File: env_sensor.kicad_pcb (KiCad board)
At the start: 2 copper layers, 43 x 63 mm, 24 parts, among them J1 E Paper, J2 ESP_Debugger, J3 Barrel_Jack, J4 LED_OUTPUT, J5 TEMP, Q1 NMOS, Q2 NMOS, Q3 NMOS, U1 MH-Z19B, U2 ESP32-DevKitC, U5 BME280

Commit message: update MOS
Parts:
- J5: value TEMP -> Conn_01x02_Pin
- Q1, Q2, Q3: footprint 2SK4017:TO230P230X650X740-3P -> env-sensor:SOT-23
- R3: value R -> 1.7k
- moved Q2 31.7 mm to (113.0, 94.7), turned to -90 degrees
- moved Q3 27.0 mm to (110.0, 98.6), turned to -90 degrees
- moved Q1 22.5 mm to (116.6, 98.3), turned to -90 degrees
- moved J4 16.0 mm to (117.6, 102.4), turned to -90 degrees
- moved C5 1.60 mm to (112.1, 72.4), turned to -90 degrees
- moved J3 1.27 mm to (124.6, 89.5)
- moved C1 0.87 mm to (111.3, 79.8)
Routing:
- net LED_C2: track 10.9 -> 31.0 mm, vias 0 -> 2
- net LED_C3: track 10.2 -> 28.1 mm, vias 0 -> 2
- net LED_V2: track 24.7 -> 6.95 mm
- net LED_C1: track 9.08 -> 25.3 mm, vias 0 -> 2
- net LED_V3: track 13.1 -> 2.80 mm
- net v12: track 24.6 -> 14.9 mm
- net LED_V1: track 10.7 -> 3.51 mm
- net GND: vias 17 -> 21

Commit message: add drv8847 (Working)
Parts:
- added R4: 330m, Resistor_SMD:R_0603_1608Metric, F.Cu at (97.5, 70.6)
- added R5: 330m, Resistor_SMD:R_0603_1608Metric, F.Cu at (97.5, 73.1)
- added U3: DRV8847SPWR, Package_SO:TSSOP-16_4.4x5mm_P0.65mm, F.Cu at (100.3, 66.1)

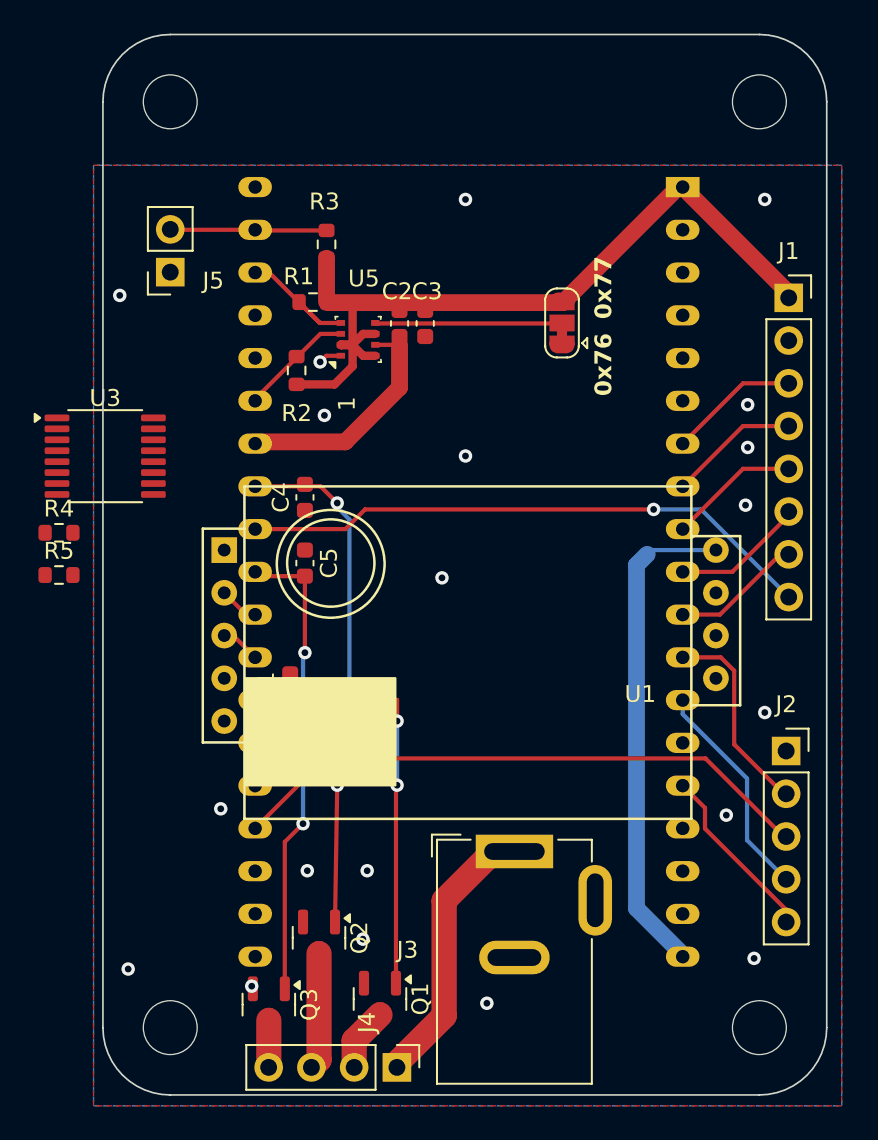
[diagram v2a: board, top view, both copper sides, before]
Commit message: add motor drivers
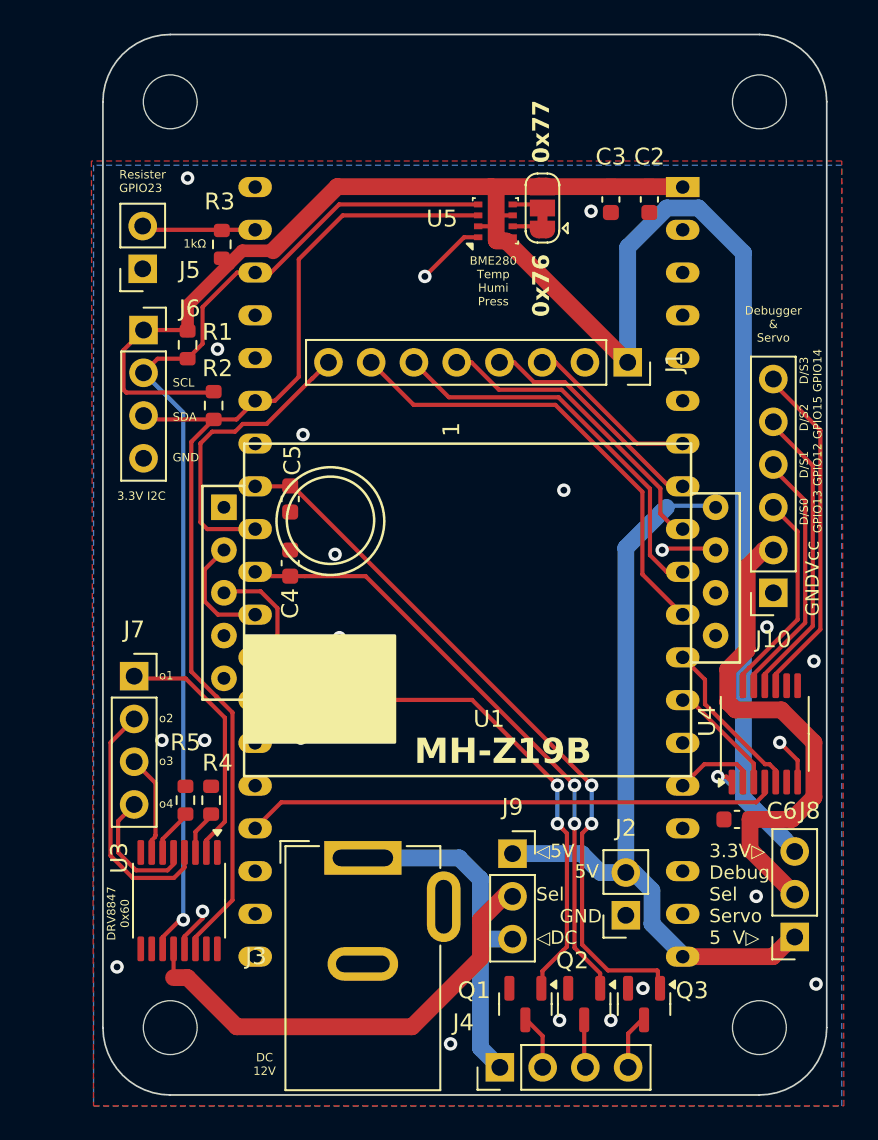
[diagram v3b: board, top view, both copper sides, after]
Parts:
- added C6: 100u, Capacitor_SMD:C_0603_1608Metric, F.Cu at (137.8, 87.6)
- added J10: Conn_01x06_Pin, Connector_PinSocket_2.54mm:PinSocket_1x06_P2.54mm_Vertical, F.Cu at (140.0, 74.2)
- added J6: Conn_01x04_Socket, Connector_PinSocket_2.54mm:PinSocket_1x04_P2.54mm_Vertical, F.Cu at (102.5, 58.6)
- added J7: Conn_01x04_Socket, Connector_PinSocket_2.54mm:PinSocket_1x04_P2.54mm_Vertical, F.Cu at (102.0, 79.1)
- added J8: v5_v3, Connector_PinSocket_2.54mm:PinSocket_1x03_P2.54mm_Vertical, F.Cu at (141.2, 94.6)
- added J9: v5_v12, Connector_PinSocket_2.54mm:PinSocket_1x03_P2.54mm_Vertical, F.Cu at (124.5, 89.7)
- added U4: TXB0104PW, Package_SO:TSSOP-14_4.4x5mm_P0.65mm, F.Cu at (139.4, 82.5)
- J2: value ESP_Debugger -> 5V_in; footprint Connector_PinSocket_2.54mm:PinSocket_1x05_P2.54mm_Vertical -> Connector_PinSocket_2.54mm:PinSocket_1x02_P2.54mm_Vertical
- moved U3 26.8 mm to (104.6, 92.5), turned to -90 degrees
- moved Q3 22.3 mm to (132.3, 98.6)
- moved R4 18.3 mm to (106.6, 86.5), turned to 90 degrees
- moved C2 16.6 mm to (132.6, 50.8)
- moved Q2 16.2 mm to (128.7, 98.6)
- moved R5 15.3 mm to (105.0, 86.5), turned to 90 degrees
- moved J2 13.6 mm to (131.2, 93.3), turned to 180 degrees
- moved C3 13.3 mm to (130.3, 50.8)
- moved U5 10.8 mm to (123.4, 52.1)
- moved J1 10.3 mm to (131.3, 60.5), turned to -90 degrees
- moved J3 9.01 mm to (115.6, 89.9)
- moved Q1 8.64 mm to (125.2, 98.6)
- moved R1 7.87 mm to (105.2, 59.4), turned to -90 degrees
- moved JP2 6.93 mm to (126.2, 51.3)
- moved R3 6.22 mm to (107.2, 53.5)
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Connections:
- J2 pad 2: AD3 -> v5v
- U2 pad 29: LED_C3 -> LED_C2
- U2 pad 31: LED_C2 -> LED_C3
- U3 pad 12: unconnected-(U3-VM-Pad12) -> Net-(J9-Pin_2)
- U3 pad 2: unconnected-(U3-OUT1-Pad2) -> Net-(J7-Pin_1)
- U3 pad 4: unconnected-(U3-OUT2-Pad4) -> Net-(J7-Pin_2)
- U3 pad 5: unconnected-(U3-OUT4-Pad5) -> Net-(J7-Pin_4)
- U3 pad 7: unconnected-(U3-OUT3-Pad7) -> Net-(J7-Pin_3)
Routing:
- net v3v: track 47.7 -> 120.3 mm, vias 0 -> 1
- net SDA: track 6.69 -> 63.0 mm
- net SCL: track 7.64 -> 61.1 mm, vias 0 -> 1
- net Net-(J10-Pin_2): track 0.00 -> 30.7 mm
- net Net-(J9-Pin_2): track 0.00 -> 27.7 mm
- net Net-(J10-Pin_6): track 0.00 -> 20.6 mm
- net EPD_RST: track 7.78 -> 27.6 mm
- net Net-(J10-Pin_5): track 0.00 -> 17.9 mm
- net v5v: track 29.0 -> 46.5 mm
- net EPD_BUSY: track 34.3 -> 17.7 mm, vias 1 -> 0
- net EPD_DC: track 7.92 -> 23.4 mm
- net Net-(J10-Pin_4): track 0.00 -> 15.3 mm
- net LED_C3: track 28.1 -> 43.2 mm
- net Net-(J7-Pin_1): track 0.00 -> 14.9 mm
- net Net-(J7-Pin_2): track 0.00 -> 14.9 mm
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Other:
- board text added: "1kΩ"
- board text added: "3.3V I2C"
- board text added: "3.3V▷ Debug Sel Servo 5 V▷"
- board text added: "5V"
- board text added: "BME280 Temp Humi Press"
- board text added: "D/S0 GPIO13"
- board text added: "D/S1 GPIO12"
- board text added: "D/S2 GPIO15"
- board text added: "D/S3 GPIO14"
- board text added: "DC 12V"
- board text added: "DRV8847 0x60"
- board text added: "Debugger & Servo"
- board text added: "GND"
- board text added: "MH-Z19B"
- board text added: "Resister GPIO23"
- board text added: "SCL"
- board text added: "SDA"
- board text added: "Vcc"
- board text added: "o1"
- board text added: "o2"
- board text added: "o3"
- board text added: "o4"
- board text added: "◁5V Sel ◁DC"

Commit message: update pcb
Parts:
- C6: value 100u -> 10u
- moved J10 8.13 mm to (140.2, 66.0)
- moved R5 3.88 mm to (106.4, 82.9), turned to -90 degrees
- moved J7 0.65 mm to (102.6, 79.0)
- moved J1 0.51 mm to (130.8, 60.5)
- moved C6 0.13 mm to (137.9, 87.6), turned to 180 degrees
- moved R4 0.13 mm to (106.4, 86.5)
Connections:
- C6 pad 1: GND -> Net-(J10-Pin_2)
- C6 pad 2: Net-(J10-Pin_2) -> GND
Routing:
- net Net-(J10-Pin_2): track 30.7 -> 39.5 mm
- net Net-(J10-Pin_3): track 12.6 -> 20.7 mm
- net Net-(J10-Pin_6): track 20.6 -> 28.6 mm
- net Net-(J10-Pin_4): track 15.3 -> 23.3 mm
- net Net-(J10-Pin_5): track 17.9 -> 26.0 mm
- net Net-(U3-ISEN34): track 2.90 -> 9.29 mm
- net EPD_RST: track 27.6 -> 25.3 mm
- net GND: track 14.8 -> 16.7 mm, vias 24 -> 27
- net EPD_DC: track 23.4 -> 21.6 mm
- net SDA: track 63.0 -> 62.4 mm
- net Net-(J7-Pin_1): track 14.9 -> 14.3 mm
- net Net-(J7-Pin_4): track 7.65 -> 8.22 mm
- net SCL: track 61.1 -> 60.6 mm
- net EPD_SCK: track 13.9 -> 14.4 mm
- net EPD_DIN: track 10.3 -> 10.9 mm

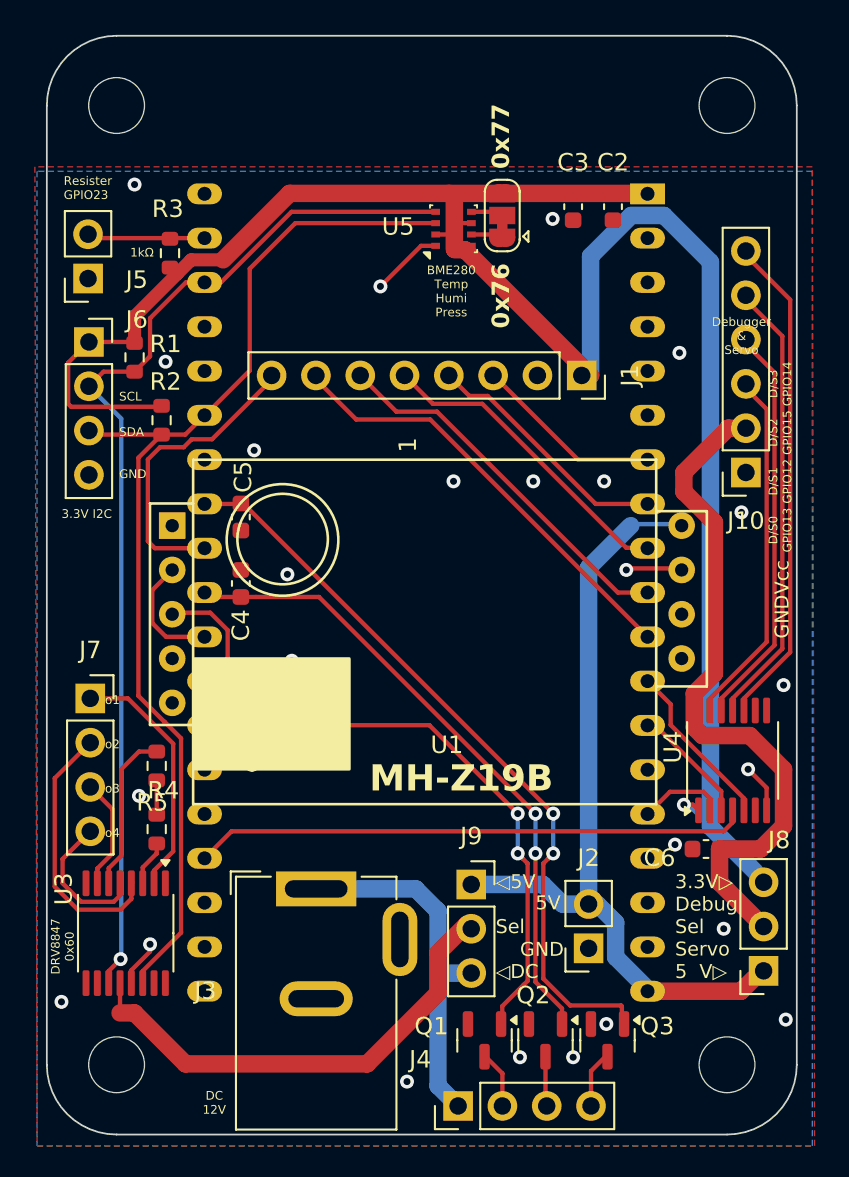
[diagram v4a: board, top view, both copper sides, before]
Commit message: delete motor driver
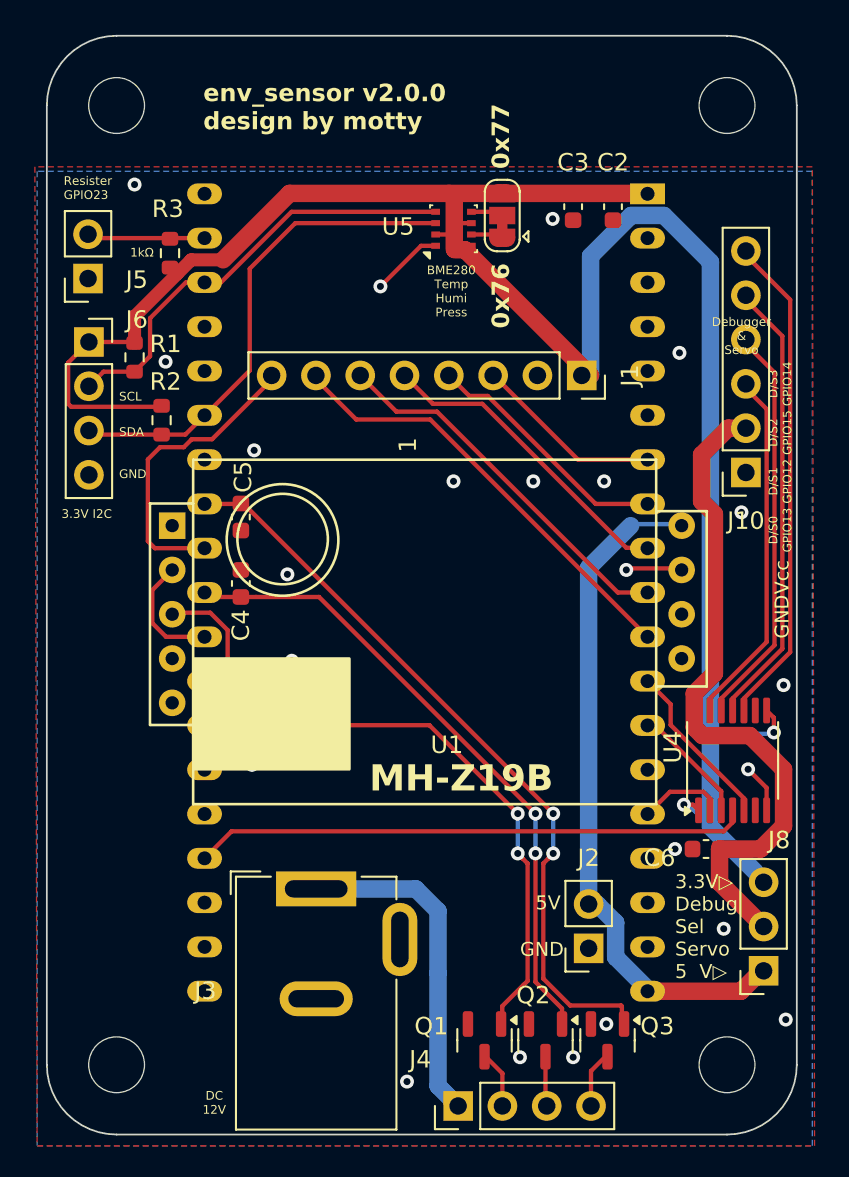
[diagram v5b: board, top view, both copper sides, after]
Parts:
- removed J7: Conn_01x04_Socket, Connector_PinSocket_2.54mm:PinSocket_1x04_P2.54mm_Vertical
- removed J9: v5_v12, Connector_PinSocket_2.54mm:PinSocket_1x03_P2.54mm_Vertical
- removed R4, R5: 330m, Resistor_SMD:R_0603_1608Metric
- removed U3: DRV8847SPWR, Package_SO:TSSOP-16_4.4x5mm_P0.65mm
- R3: value 1.7k -> 1k
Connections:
- U4 pad 8: unconnected-(U4-OE-Pad8) -> v3v
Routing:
- net SCL: track 60.6 -> 25.3 mm, vias 1 -> 0
- net SDA: track 62.4 -> 28.4 mm
- net Net-(J9-Pin_2): track 27.7 -> 0.00 mm
- net Net-(J7-Pin_2): track 15.3 -> 0.00 mm
- net Net-(J7-Pin_1): track 14.3 -> 0.00 mm
- net Net-(U3-ISEN34): track 9.29 -> 0.00 mm
- net Net-(J7-Pin_4): track 8.22 -> 0.00 mm
- net v5v: track 46.5 -> 39.3 mm
- net Net-(J7-Pin_3): track 6.40 -> 0.00 mm
- net v3v: track 120.3 -> 125.4 mm, vias 1 -> 2
- net GND: track 16.7 -> 12.1 mm, vias 27 -> 24
- net Net-(U3-ISEN12): track 2.61 -> 0.00 mm
- net v12: track 21.6 -> 19.4 mm
- net Net-(J10-Pin_2): track 39.5 -> 38.7 mm
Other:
- board text added: "env_sensor v2.0.0 design by motty"
- board text removed: "DRV8847 0x60"
- board text removed: "o1"
- board text removed: "o2"
- board text removed: "o3"
- board text removed: "o4"
- board text removed: "◁5V Sel ◁DC"

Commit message: update
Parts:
- removed J2: 5V_in, Connector_PinSocket_2.54mm:PinSocket_1x02_P2.54mm_Vertical
- removed J8: v5_v3, Connector_PinSocket_2.54mm:PinSocket_1x03_P2.54mm_Vertical
- removed U2: ESP32-DevKitC, Espressif:ESP32-DevKitC
- added C10: 10u/10V, Capacitor_SMD:C_0603_1608Metric, F.Cu at (101.4, 80.6)
- added C11: 1u/10V, Capacitor_SMD:C_0603_1608Metric, F.Cu at (107.1, 78.6)
- added C12: 4.7u/6.3V, Capacitor_SMD:C_0603_1608Metric, F.Cu at (118.2, 86.8)
- added C13: 15p, Capacitor_SMD:C_0603_1608Metric, F.Cu at (110.1, 60.3)
- added C14: 15p, Capacitor_SMD:C_0603_1608Metric, F.Cu at (106.5, 58.6)
- added C7: 0.1u, Capacitor_SMD:C_0603_1608Metric, F.Cu at (110.2, 49.7)
- added C8: 0.01u, Capacitor_SMD:C_0603_1608Metric, F.Cu at (110.2, 52.7)
- added C9: 0.1u/10v, Capacitor_SMD:C_0603_1608Metric, F.Cu at (101.4, 77.6)
- added D1: D_Schottky, Diode_SMD:D_SMA, F.Cu at (111.6, 80.5)
- added D2: D_Schottky, Diode_SMD:D_SMA, F.Cu at (111.5, 84.1)
- added D3: D_Schottky, Diode_SMD:D_SMA, F.Cu at (118.9, 84.1)
- added D4: POWER, LED_SMD:LED_0603_1608Metric, F.Cu at (110.1, 56.3)
- added J7: USB_C_Receptacle_USB2.0_16P, Connector_USB:USB_C_Receptacle_GCT_USB4105-xx-A_16P_TopMnt_Horizontal, F.Cu at (103.7, 65.7)
- added J9: DEBUG, Connector_PinSocket_2.54mm:PinSocket_1x05_P2.54mm_Vertical, F.Cu at (138.1, 55.7)
- added R4: 10k, Resistor_SMD:R_0603_1608Metric, F.Cu at (110.2, 51.2)
- added R5: 5.1k, Resistor_SMD:R_0603_1608Metric, F.Cu at (110.2, 67.4)
- added R6: 5.1k, Resistor_SMD:R_0603_1608Metric, F.Cu at (110.1, 64.3)
- added R7: 1k, Resistor_SMD:R_0603_1608Metric, F.Cu at (107.0, 56.3)
- added U3: ESP32-S3-WROOM-1, RF_Module:ESP32-S3-WROOM-1, F.Cu at (121.5, 55.3)
- added U6: TPS2065CDBV, Package_TO_SOT_SMD:SOT-23-5, F.Cu at (104.0, 78.1)
- added U7: AP7361C-33E, Package_TO_SOT_SMD:SOT-223-3_TabPin2, F.Cu at (118.9, 77.9)
- added Y1: Crystal, Crystal:Crystal_SMD_3215-2Pin_3.2x1.5mm, F.Cu at (109.3, 58.3)
- J10: value Conn_01x06_Pin -> PWMOUT
- J5: value Conn_01x02_Pin -> RegSense
- J6: value Conn_01x04_Socket -> I2c
- JP2: value SolderJumper_3_Bridged12 -> Default77
- moved J6 54.7 mm to (123.6, 109.1), turned to 90 degrees
- moved R1 49.7 mm to (131.1, 101.8), turned to 0 degrees
- moved JP2 49.4 mm to (133.0, 100.2)
- moved C2 46.9 mm to (134.2, 97.7), turned to 0 degrees
- moved C3 45.3 mm to (134.2, 95.9), turned to 0 degrees
- moved U5 44.9 mm to (130.6, 96.4), turned to 0 degrees
- moved R2 43.5 mm to (128.2, 100.9), turned to 0 degrees
- moved J5 35.7 mm to (138.1, 53.2)
- moved J10 27.9 mm to (138.1, 93.8)
- moved U1 27.6 mm to (134.3, 77.3), turned to 0 degrees
- moved R3 26.0 mm to (133.0, 50.7), turned to 0 degrees
- moved Q3 24.2 mm to (109.9, 89.4), turned to 180 degrees
- moved J1 21.9 mm to (111.9, 71.6), turned to 90 degrees
- moved C5 21.0 mm to (112.6, 89.5), turned to -90 degrees
- moved C4 20.7 mm to (112.6, 93.0)
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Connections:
- J1 pad 3: EPD_DIN -> SPI_MOSI
- J1 pad 4: EPD_SCK -> SPI_SCLK
- J1 pad 5: EPD_CS -> EPD_ChipSelect
- J1 pad 6: EPD_DC -> EPD_DataControl
- J1 pad 8: EPD_BUSY -> EPD_BackLight
- U1 pad 2: TX(ESP_UP) -> RX(ESP_DOWN)
- U1 pad 3: RX(ESP_DOWN) -> TX(ESP_UP)
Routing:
- net v3v: track 125.4 -> 6.61 mm, vias 2 -> 1
- net LED_C3: track 43.2 -> 0.00 mm, vias 2 -> 0
- net v5v: track 39.3 -> 0.00 mm
- net LED_C2: track 36.9 -> 0.00 mm, vias 2 -> 0
- net LED_C1: track 33.0 -> 0.00 mm, vias 2 -> 0
- net AD2: track 31.8 -> 0.00 mm
- net SDA: track 28.4 -> 0.00 mm
- net EPD_RST: track 25.3 -> 0.00 mm
- net SCL: track 25.3 -> 0.00 mm
- net EPD_DC: track 21.6 -> 0.00 mm
- net v12: track 19.4 -> 0.00 mm
- net EPD_CS: track 17.6 -> 0.00 mm
- net EPD_BUSY: track 17.3 -> 0.00 mm
- net Net-(J10-Pin_6): track 28.6 -> 12.8 mm
- net EPD_SCK: track 14.4 -> 0.00 mm
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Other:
- board size 43 x 63 mm -> 102.9 x 143 mm
- board text added: "${REFERENCE}"
- board text removed: "0x76"
- board text removed: "0x77"
- board text removed: "1"
- board text removed: "1kΩ"
- board text removed: "3.3V I2C"
- board text removed: "3.3V▷ Debug Sel Servo 5 V▷"
- board text removed: "5V"
- board text removed: "BME280 Temp Humi Press"
- board text removed: "D/S0 GPIO13"
- board text removed: "D/S1 GPIO12"
- board text removed: "D/S2 GPIO15"
- board text removed: "D/S3 GPIO14"
- board text removed: "DC 12V"
- board text removed: "Debugger & Servo"
- board text removed: "GND"
- board text removed: "MH-Z19B"
- board text removed: "Resister GPIO23"
- board text removed: "SCL"
- board text removed: "SDA"
- board text removed: "Vcc"
